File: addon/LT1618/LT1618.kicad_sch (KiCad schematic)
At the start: 12 parts

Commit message: Chore: routed LT1618 addon board
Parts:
- added J1, J2: Conn_01x04, Connector_PinHeader_2.54mm:PinHeader_1x04_P2.54mm_Vertical, symbol Connector_Generic:Conn_01x04
- C1, C2, C3: renamed from C?; footprint (none) -> Resistor_SMD:R_0805_2012Metric_Pad1.20x1.40mm_HandSolder; Order Code (none) -> -; Supplier (none) -> Mouser
- D1: renamed from D?; footprint (none) -> Diode_SMD:D_SMB_Handsoldering; Order Code (none) -> 583-FM240A; Supplier (none) -> Mouser
- L1: renamed from L?; footprint (none) -> Inductor_THT:L_Radial_D7.2mm_P3.00mm_Murata_1700; Order Code (none) -> 652-RLB0712-100KL; Supplier (none) -> Mouser
- R1, R2, R3, R4, R5, R6: renamed from R?; footprint (none) -> Resistor_SMD:R_0805_2012Metric_Pad1.20x1.40mm_HandSolder; Order Code (none) -> -; Supplier (none) -> Mouser
- U1: renamed from U?; footprint (none) -> Package_SO:MSOP-10_3x3mm_P0.5mm; Order Code (none) -> 584-LT1618EMS#TRPBF; Supplier (none) -> Mouser
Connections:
- net GND: now also J1.3 (Pin_3), J1.4 (Pin_4), J2.3 (Pin_3), J2.4 (Pin_4)
- net at C1.1, R1.1, R3.1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: now also J1.1 (Pin_1), J1.2 (Pin_2)
- net +15V: no longer names the net of C3.1, D1.1 (K), R4.1
- net +15V: now also J2.1 (Pin_1), J2.2 (Pin_2)
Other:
- note added: "Input connector"
- note added: "Output connector"

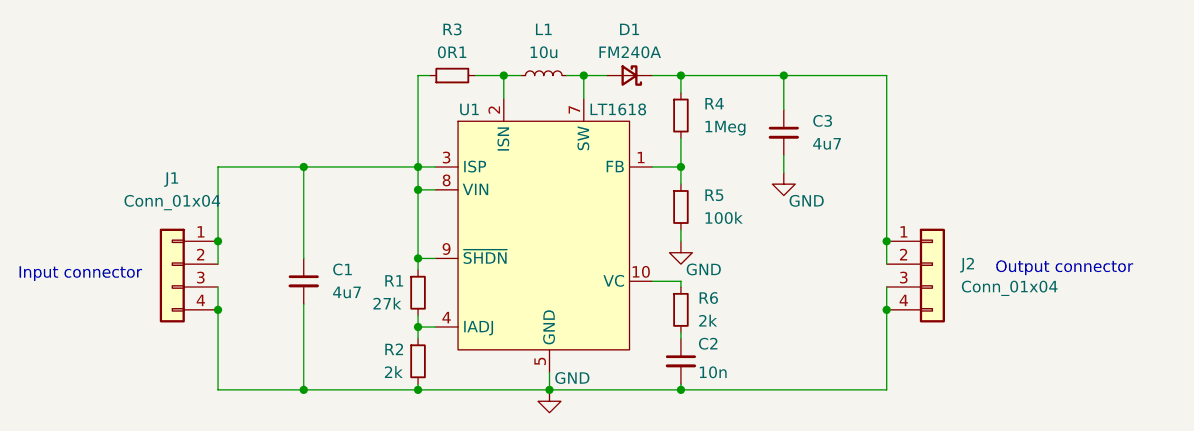
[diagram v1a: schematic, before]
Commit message: Fix: changed out inductor and flipped pin headers
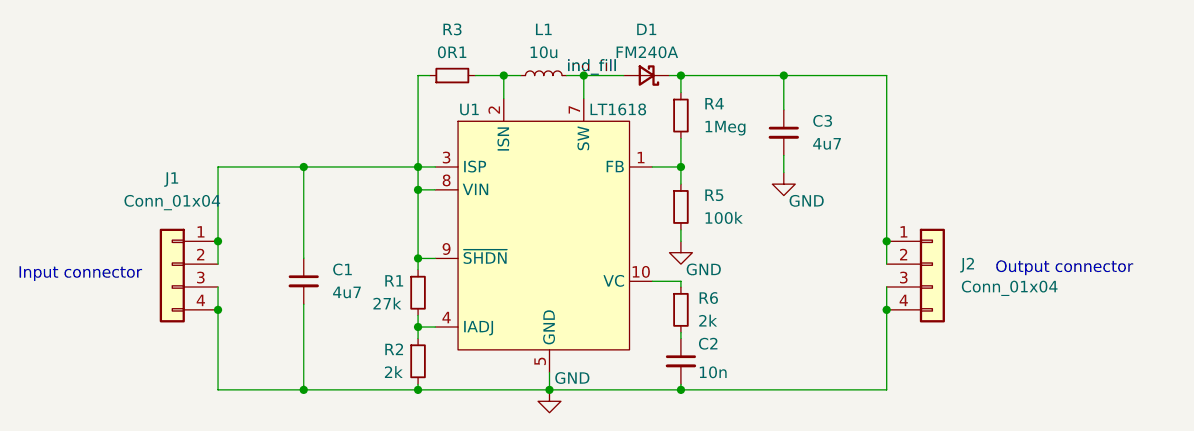
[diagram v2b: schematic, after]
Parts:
- L1: footprint Inductor_THT:L_Radial_D7.2mm_P3.00mm_Murata_1700 -> Inductor_SMD:L_Bourns_SRN6045TA; Order Code 652-RLB0712-100KL -> 810-VLS5045EX-100M
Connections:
- net ind_fill: now reaches D1.2 (A), L1.2, U1.7 (SW)
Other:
- moved on the sheet: D1
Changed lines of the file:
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@@
     (stroke (width 0) (type default) (color 0 0 0 0))
   )
-  (wire (pts (xy 126.365 81.28) (xy 128.905 81.28))
+  (wire (pts (xy 126.365 81.28) (xy 130.81 81.28))
     (stroke (width 0) (type default) (color 0 0 0 0))
   )
@@
     (stroke (width 0) (type default) (color 0 0 0 0))
   )
-  (wire (pts (xy 133.985 81.28) (xy 137.16 81.28))
+  (wire (pts (xy 135.89 81.28) (xy 137.16 81.28))
     (stroke (width 0) (type default) (color 0 0 0 0))
   )
@@
     (effects (font (size 1.27 1.27)) (justify left bottom))
   )
-  (symbol (lib_id "Device:D_Schottky_Small") (at 131.445 81.28 180) (unit 1)
-    (in_bom yes) (on_board yes)
-    (property "Reference" "D1" (id 0) (at 131.445 76.2 0))
-    (property "Value" "FM240A" (id 1) (at 131.445 78.74 0))
-    (property "Footprint" "Diode_SMD:D_SMB_Handsoldering" (id 2) (at 131.445 81.28 90)
-      (effects (font (size 1.27 1.27)) hide)
-    )
-    (property "Datasheet" "~" (id 3) (at 131.445 81.28 90)
-      (effects (font (size 1.27 1.27)) hide)
-    )
-    (property "Supplier" "Mouser" (id 4) (at 131.445 81.28 0)
-      (effects (font (size 1.27 1.27)) hide)
-    )
-    (property "Order Code" "583-FM240A" (id 5) (at 131.445 81.28 0)
+  (label "ind_fill" (at 124.46 81.28 0)
+    (effects (font (size 1.27 1.27)) (justify left bottom))
+  )
+  (symbol (lib_id "Device:D_Schottky_Small") (at 133.35 81.28 180) (unit 1)
+    (in_bom yes) (on_board yes)
+    (property "Reference" "D1" (id 0) (at 133.35 76.2 0))
+    (property "Value" "FM240A" (id 1) (at 133.35 78.74 0))
+    (property "Footprint" "Diode_SMD:D_SMB_Handsoldering" (id 2) (at 133.35 81.28 90)
+      (effects (font (size 1.27 1.27)) hide)
+    )
+    (property "Datasheet" "~" (id 3) (at 133.35 81.28 90)
+      (effects (font (size 1.27 1.27)) hide)
+    )
+    (property "Supplier" "Mouser" (id 4) (at 133.35 81.28 0)
+      (effects (font (size 1.27 1.27)) hide)
+    )
+    (property "Order Code" "583-FM240A" (id 5) (at 133.35 81.28 0)
       (effects (font (size 1.27 1.27)) hide)
     )
@@
     (property "Reference" "L1" (id 0) (at 121.92 76.2 90))
     (property "Value" "10u" (id 1) (at 121.92 78.74 90))
-    (property "Footprint" "Inductor_THT:L_Radial_D7.2mm_P3.00mm_Murata_1700" (id 2) (at 121.92 81.28 0)
+    (property "Footprint" "Inductor_SMD:L_Bourns_SRN6045TA" (id 2) (at 121.92 81.28 0)
       (effects (font (size 1.27 1.27)) hide)
     )
@@
       (effects (font (size 1.27 1.27)) hide)
     )
-    (property "Order Code" "652-RLB0712-100KL" (id 4) (at 121.92 81.28 0)
+    (property "Order Code" "810-VLS5045EX-100M" (id 4) (at 121.92 81.28 0)
       (effects (font (size 1.27 1.27)) hide)
     )
@@
     )
     (path "/8847e751-6992-4f80-92c5-c3bef4b5dbf6"
-      (reference "L1") (unit 1) (value "10u") (footprint "Inductor_THT:L_Radial_D7.2mm_P3.00mm_Murata_1700")
+      (reference "L1") (unit 1) (value "10u") (footprint "Inductor_SMD:L_Bourns_SRN6045TA")
     )
     (path "/cdb2878b-f702-4635-9e4c-1cc8cfe5a84c"
